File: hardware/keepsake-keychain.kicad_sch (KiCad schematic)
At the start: 45 parts, among them Q1 MMFTP4042K, Q2 MMFTP4042K, Q3 MMFTP4042K, Q4 MMFTP4042K, SW1 SPDT Power Switch, SW2 R-667842, U1 3SM123C4T1QA, U1 ATTINY1614, U2 74HC595 RED Shift Register, U3 74HC595 GREEN Shift Register, U4 74HC595 BLUE Shift Register

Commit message: Add op-amp
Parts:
- added C1, C2: 0.1uF, symbol Device:C_Small
- added D1: BAT54, BAT54:SOT95P240X120-3N, symbol 0_Schottky_Diode:BAT54
- added U6: MCP6001, SOT-23-5_MC_MCH, symbol 0_Op_Amp:MCP6001T-I_OT
- renumbered U1 to U5
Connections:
- net GND: now also C1.1, U6.2 (VSS)
- net at U1.9 (PB0): no longer SW2.1
- net 3V renamed +3V3
- net +3V3: now also C1.2, C2.1
- new net: C2.2, U6.5 (VDD)
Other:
- note removed: "Add decoupling cap 0.1µF ceramic, get footprint size"
- moved on the sheet: BT1, SW1, SW2

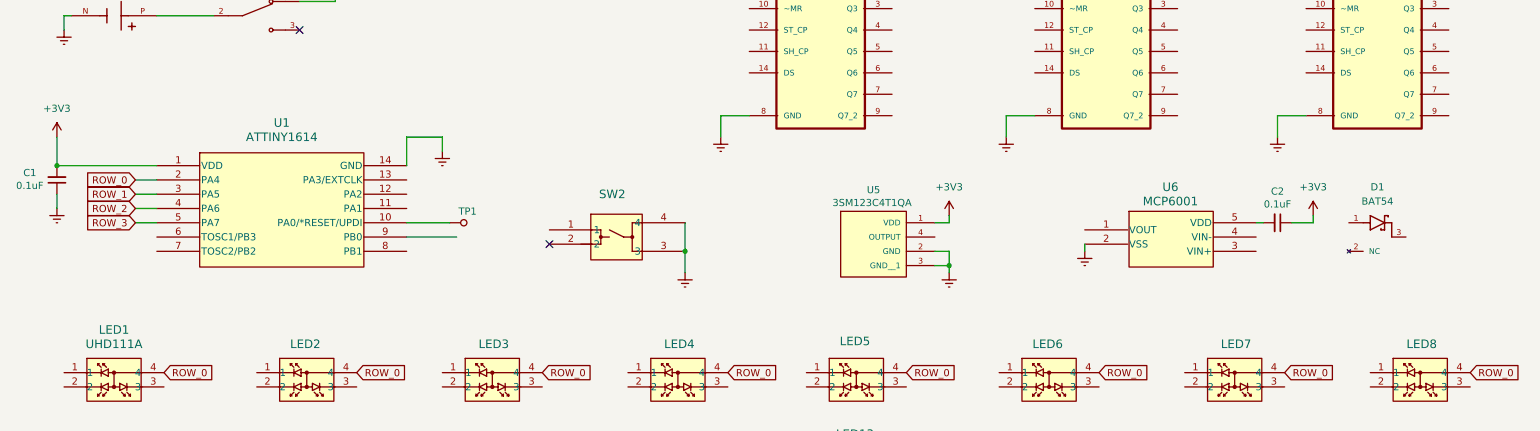
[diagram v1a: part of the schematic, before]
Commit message: Add filtering and label nets
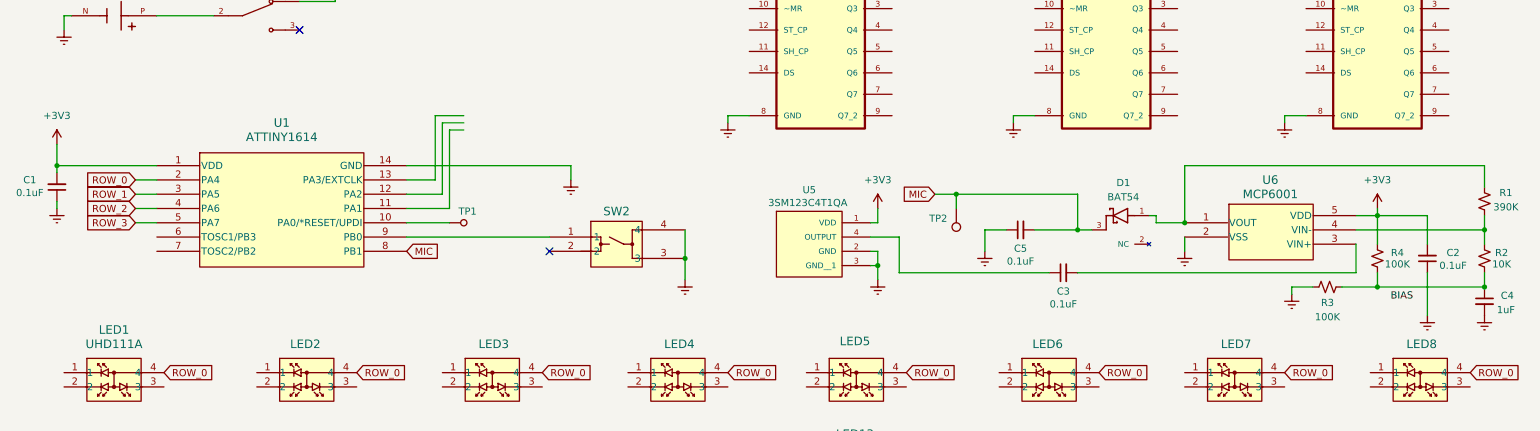
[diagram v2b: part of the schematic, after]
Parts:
- added C3, C5: 0.1uF, symbol Device:C_Small
- added C4: 1uF, symbol Device:C_Small
- added R1: 390K, Resistor_SMD:R_0603_1608Metric_Pad0.98x0.95mm_HandSolder, symbol Device:R_Small_US
- added R2: 10K, Resistor_SMD:R_0603_1608Metric_Pad0.98x0.95mm_HandSolder, symbol Device:R_Small_US
- added R3, R4: 100K, Resistor_SMD:R_0603_1608Metric_Pad0.98x0.95mm_HandSolder, symbol Device:R_Small_US
- added TP2: TestPoint, TestPoint:TestPoint_Pad_D1.0mm, symbol Connector:TestPoint
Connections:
- net +3V3: now also C2.2, U6.5 (VDD), R4.1; no longer C2.1
- net GND: now also C2.1, C4.2, C5.1, R3.2
- net MIC: now reaches U1.8 (PB1)
- net MIC: now also D1.3, C5.2, TP2.1
- net at U1.9 (PB0): now also SW2.1
- net at U6.1 (VOUT): now also D1.1, R1.1
- net at U6.3 (VIN+): now also C3.2
- net at U6.4 (VIN-): now also R1.2, R2.1
- net at U5.4 (OUTPUT): now also C3.1
- new net: C4.1, R2.2, R3.1, R4.2
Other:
- moved on the sheet: C1, C2, D1, SW2, U5, U6

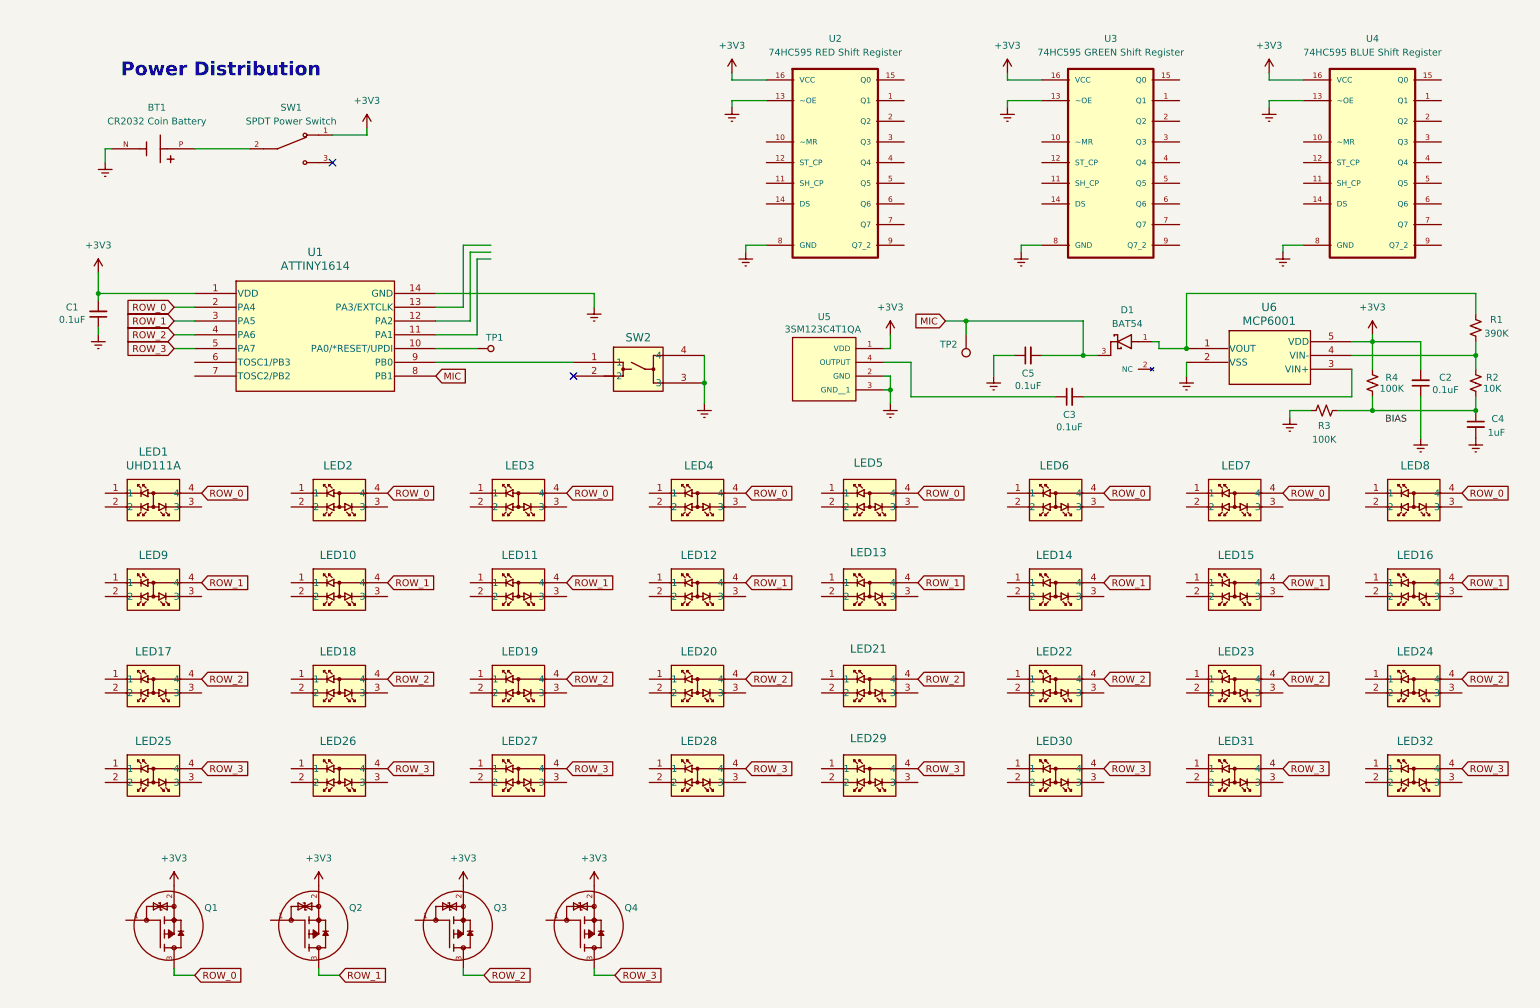
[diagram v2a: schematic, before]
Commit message: Continue schematic stweaks, connect nets
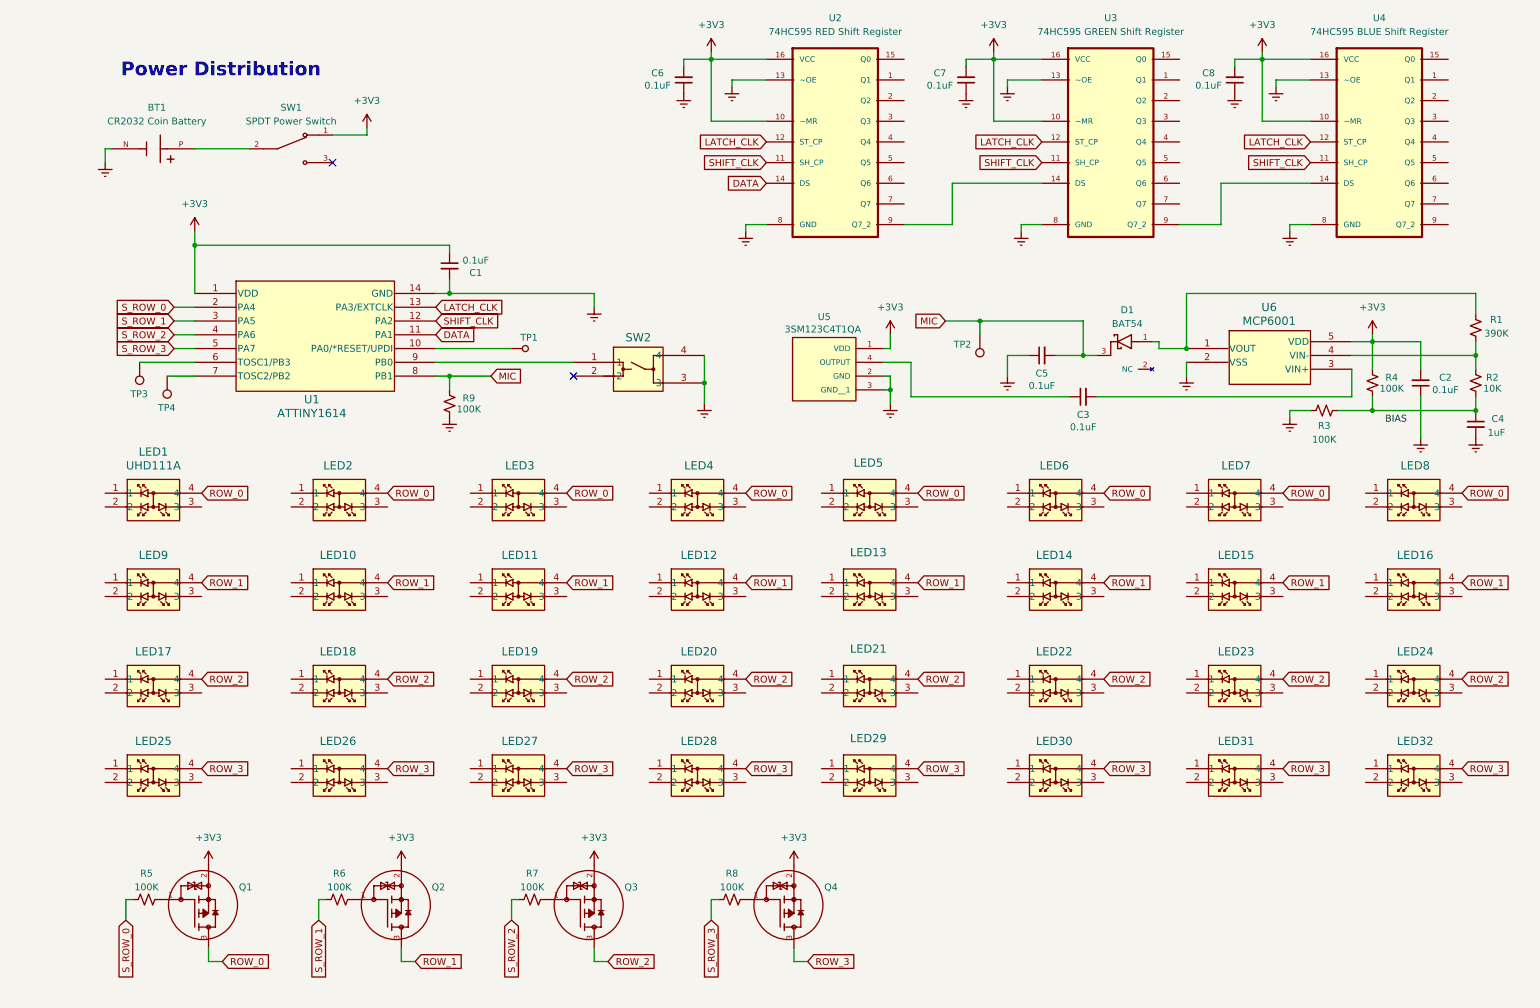
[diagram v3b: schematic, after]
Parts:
- added C6, C7, C8: 0.1uF, symbol Device:C_Small
- added R5, R6, R7, R8, R9: 100K, Resistor_SMD:R_0603_1608Metric_Pad0.98x0.95mm_HandSolder, symbol Device:R_Small_US
- added TP3, TP4: TestPoint, Connector_Pin:Pin_D1.0mm_L10.0mm, symbol Connector:TestPoint
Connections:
- net +3V3: now also C1.1, U2.10 (~MR), U3.10 (~MR), U4.10 (~MR), C6.2, C7.2, C8.2; no longer C1.2
- net GND: now also C1.2, C6.1, C7.1, C8.1, R9.2; no longer C1.1
- net MIC: now also R9.1
- net ROW_0: no longer U1.2 (PA4)
- net ROW_1: no longer U1.3 (PA5)
- net ROW_2: no longer U1.4 (PA6)
- net ROW_3: no longer U1.5 (PA7)
- net DATA: now reaches U1.11 (PA1)
- net DATA: now also U2.14 (DS)
- net SHIFT_CLK: now reaches U1.12 (PA2)
- net SHIFT_CLK: now also U2.11 (SH_CP), U3.11 (SH_CP), U4.11 (SH_CP)
- net LATCH_CLK: now reaches U1.13 (PA3/EXTCLK)
- net LATCH_CLK: now also U2.12 (ST_CP), U3.12 (ST_CP), U4.12 (ST_CP)
- net at U1.6 (TOSC1/PB3): now also TP3.1
- net at U1.7 (TOSC2/PB2): now also TP4.1
- net at U4.14 (DS): now also U3.9 (Q7_2)
- net at Q1.1: now also R5.2
- net at Q3.1: now also R7.2
- net at Q2.1: now also R6.2
- net at U2.9 (Q7_2): now also U3.14 (DS)
- net at Q4.1: now also R8.2
- new net S_ROW_0: R5.1, U1.2 (PA4)
- new net S_ROW_1: R6.1, U1.3 (PA5)
- new net S_ROW_2: R7.1, U1.4 (PA6)
- new net S_ROW_3: R8.1, U1.5 (PA7)
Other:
- moved on the sheet: C1, C3, C5, Q1, Q2, Q3, Q4, TP1, TP2, U2, U3, U4

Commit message: Replace tactile button and power switch for space conservancy
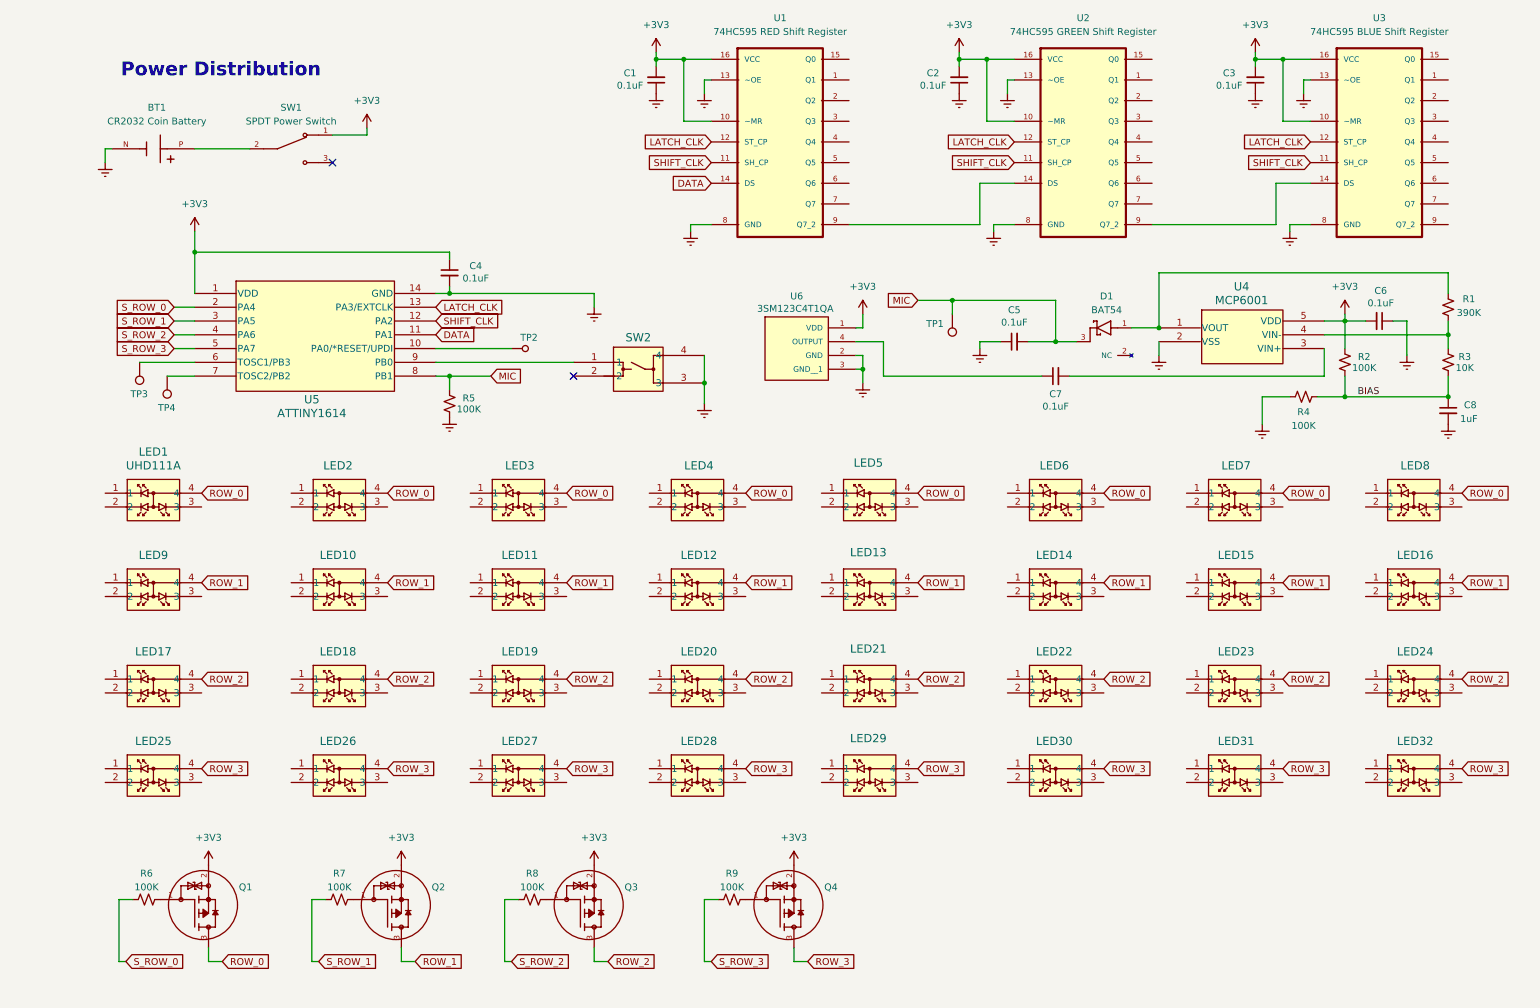
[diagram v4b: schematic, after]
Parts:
- SW1: footprint 0_SPDT_Switch:spdt-switch -> SLW-129956-4A-RA-N-D:SW_SLW-129956-4A-RA-N-D
- renumbered C6 to C1, C7 to C2, C8 to C3, C1 to C4, C2 to C6, C3 to C7, C4 to C8, R4 to R2, R2 to R3, R3 to R4, R9 to R5, R5 to R6, R6 to R7, R7 to R8, R8 to R9, TP2 to TP1, TP1 to TP2, U2 to U1, U3 to U2, U4 to U3, U6 to U4, U1 to U5, U5 to U6
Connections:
- net BIAS: now also C8.1, R2.2, R3.2, R4.1
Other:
- moved on the sheet: C1, C2, C3, C4, C5, C6, C7, C8, D1, R1, R2, R3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

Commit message: Upgrade CR2032 to CR2450 for longer battery life
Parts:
- BT1: footprint digikey-footprints:Battery_Holder_Coin_2032_BS-7 -> 0_Coin_Battery_Holder:battery-holder
- C1, C2, C3, C4, C5, C6, C7, C8: footprint (none) -> Capacitor_SMD:C_0603_1608Metric_Pad1.08x0.95mm_HandSolder
- D1: footprint BAT54:SOT95P240X120-3N -> 0_Schottky_Diode:SOT95P240X120-3N
- SW1: footprint SLW-129956-4A-RA-N-D:SW_SLW-129956-4A-RA-N-D -> 0_SPDT_Switch:spdt-switch
- SW2: footprint R-667_MIT -> 0_Push_Button:SW_PTS636_SK25J_SMTR_LFS_CNK-M
- U4: footprint SOT-23-5_MC_MCH -> 0_Op_Amp:SOT-23-5_MC_MCH
- U6: footprint 3SM123C4T1QA:MIC_3SM123C4T1QA -> 0_Microphone:MIC_3SM123C4T1QA
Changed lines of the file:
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@@
 			)
 		)
-		(property "Footprint" ""
+		(property "Footprint" "Capacitor_SMD:C_0603_1608Metric_Pad1.08x0.95mm_HandSolder"
 			(at 271.78 87.63 0)
 			(effects
@@
 			)
 		)
-		(property "Footprint" ""
+		(property "Footprint" "Capacitor_SMD:C_0603_1608Metric_Pad1.08x0.95mm_HandSolder"
 			(at 87.63 62.23 0)
 			(effects
@@
 			)
 		)
-		(property "Footprint" ""
+		(property "Footprint" "Capacitor_SMD:C_0603_1608Metric_Pad1.08x0.95mm_HandSolder"
 			(at 191.77 74.93 0)
 			(effects
@@
 			)
 		)
-		(property "Footprint" ""
+		(property "Footprint" "Capacitor_SMD:C_0603_1608Metric_Pad1.08x0.95mm_HandSolder"
 			(at 125.73 26.67 0)
 			(effects
@@
 			)
 		)
-		(property "Footprint" "SOT-23-5_MC_MCH"
+		(property "Footprint" "0_Op_Amp:SOT-23-5_MC_MCH"
 			(at 233.68 73.66 0)
 			(effects
@@
 			)
 		)
-		(property "Footprint" "SLW-129956-4A-RA-N-D:SW_SLW-129956-4A-RA-N-D"
+		(property "Footprint" "0_SPDT_Switch:spdt-switch"
 			(at 58.42 39.37 0)
 			(effects
@@
 			)
 		)
-		(property "Footprint" ""
+		(property "Footprint" "Capacitor_SMD:C_0603_1608Metric_Pad1.08x0.95mm_HandSolder"
 			(at 181.61 26.67 0)
 			(effects
@@
 			)
 		)
-		(property "Footprint" "BAT54:SOT95P240X120-3N"
+		(property "Footprint" "0_Schottky_Diode:SOT95P240X120-3N"
 			(at 208.28 74.93 0)
 			(effects
@@
 			)
 		)
-		(property "Footprint" ""
+		(property "Footprint" "Capacitor_SMD:C_0603_1608Metric_Pad1.08x0.95mm_HandSolder"
 			(at 259.08 71.12 0)
 			(effects
@@
 			)
 		)
-		(property "Footprint" "3SM123C4T1QA:MIC_3SM123C4T1QA"
+		(property "Footprint" "0_Microphone:MIC_3SM123C4T1QA"
 			(at 151.13 76.2 0)
 			(effects
@@
 			)
 		)
-		(property "Footprint" "digikey-footprints:Battery_Holder_Coin_2032_BS-7"
+		(property "Footprint" "0_Coin_Battery_Holder:battery-holder"
 			(at 33.02 39.37 0)
 			(effects
@@
 			)
 		)
-		(property "Footprint" "R-667_MIT"
+		(property "Footprint" "0_Push_Button:SW_PTS636_SK25J_SMTR_LFS_CNK-M"
 			(at 121.92 80.01 0)
 			(effects
@@
 			)
 		)
-		(property "Footprint" ""
+		(property "Footprint" "Capacitor_SMD:C_0603_1608Metric_Pad1.08x0.95mm_HandSolder"
 			(at 236.22 26.67 0)
 			(effects
@@
 			)
 		)
-		(property "Footprint" ""
+		(property "Footprint" "Capacitor_SMD:C_0603_1608Metric_Pad1.08x0.95mm_HandSolder"
 			(at 199.39 81.28 0)
 			(effects

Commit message: Assign footprints to components
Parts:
- removed BT1: CR2032 Coin Battery, 0_Coin_Battery_Holder:battery-holder, symbol 0_Coin_Battery_Holder:BH-25C-1
- removed SW2: R-667842, 0_Push_Button:SW_PTS636_SK25J_SMTR_LFS_CNK-M, symbol 0_Tactile_Push_Button:R-667842
- removed TP1: TestPoint, TestPoint:TestPoint_Pad_D1.0mm, symbol Connector:TestPoint
- removed TP3, TP4: TestPoint, Connector_Pin:Pin_D1.0mm_L10.0mm, symbol Connector:TestPoint
- added BT1: CR2450 Coin Battery, 0_Coin_Battery_Holder:battery-holder, symbol 0_Coin_Battery_Holder:BHX1-2450-SM
- added SW2: PTS636 SK25J SMTR LFS, 0_SPDT_Switch:spdt-switch, symbol 0_Tactile_Push_Button:PTS636_SK25J_SMTR_LFS
- added TP1, TP3, TP4: 5002, digikey-footprints:Test_Point_D1.02mm, symbol dk_Test-Points:5002
- U4: value MCP6001 -> Op Amp
- U5: footprint 0_ATtiny1614:SOIC14_SL_MCH-M -> 0_ATtiny1614:SOIC14_SL_MCH
- U6: value 3SM123C4T1QA -> MEMS Microphone
- renumbered C6 to C5, C5 to C6
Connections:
- net GND: now also BT1.2, SW2.2
- net MIC: now also TP1.1
- net at U5.6 (TOSC1/PB3): now also TP3.1
- net at U5.7 (TOSC2/PB2): now also TP4.1
- net at U5.9 (PB0): now also SW2.1
- net at SW1.2: now also BT1.1, BT1.1_1
- no-connect marks 2 -> 1
